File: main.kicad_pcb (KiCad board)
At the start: 2 copper layers, 100.2 x 114.2 mm, 82 parts, among them J1 Screw_Terminal_01x02, J2 Screw_Terminal_01x10, Q1 IRF540N, Q2 IRF540N, Q3 IRF540N, Q4 IRF540N, Q5 IRF540N, SW1 Arduino Reset, SW10 func3, SW11 func4, SW12 func5, SW13 Button_STOP, SW2 Switch_All, SW3 Switch1, SW4 Switch2, SW5 Switch3, SW6 Switch4, SW7 Switch5, SW8 func1, SW9 func2, U1 L7805, U2 ATmega328P-PU, U3 PC817, U4 PC817, U5 PC817, U6 PC817, U7 PC817, Y1 16mHz

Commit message: change layout
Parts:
- added H1: MountingHole, MountingHole:MountingHole_2.5mm_Pad, F.Cu at (51.6, 27.2)
- added H2: MountingHole, MountingHole:MountingHole_2.5mm_Pad, F.Cu at (135.6, 27.2)
- added H3: MountingHole, MountingHole:MountingHole_2.5mm_Pad, F.Cu at (51.6, 132.0)
- added H4: MountingHole, MountingHole:MountingHole_2.5mm_Pad, F.Cu at (135.6, 131.7)
- moved C1 57.9 mm to (65.2, 66.7)
- moved C6 57.9 mm to (65.2, 71.7)
- moved U1 57.9 mm to (70.7, 66.7)
- moved SW2 52.7 mm to (71.6, 126.7)
- moved R41 47.4 mm to (93.1, 53.1)
- moved R38 46.9 mm to (89.1, 75.7)
- moved Q5 46.9 mm to (91.0, 46.4)
- moved U7 46.9 mm to (89.2, 72.9)
- moved R39 46.9 mm to (89.1, 61.1)
- moved R40 46.9 mm to (89.1, 55.3)
- moved R42 46.9 mm to (89.1, 52.4)
- moved D5 46.9 mm to (89.1, 58.2)
- moved R18 44.9 mm to (132.7, 75.7)
- moved U3 44.9 mm to (132.7, 72.2)
- moved Q1 44.9 mm to (134.6, 46.4)
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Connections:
- J2 pad 1: /LED5 -> /LED1
- J2 pad 3: /LED4 -> /LED2
- J2 pad 7: /LED2 -> /LED4
- J2 pad 9: /LED1 -> /LED5
- SW13 pad 1: /Button_STOP -> GNDS
- SW13 pad 2: GNDS -> /Button_STOP
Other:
- board size 100.2 x 114.2 mm -> 95 x 114.2 mm
- board text added: "12V"
- board text added: "2021/09/26"
- board text added: "Arduino Reset"
- board text added: "Func Stop"
- board text added: "Func1"
- board text added: "Func2"
- board text added: "Func3"
- board text added: "Func4"
- board text added: "Func5"
- board text added: "GND"
- board text added: "LED-SW-ALL"
- board text added: "LED1"
- board text added: "LED1-SW"
- board text added: "LED1-VR"
- board text added: "LED2"
- board text added: "LED2-SW"
- board text added: "LED2-VR"
- board text added: "LED3"
- board text added: "LED3-SW"
- board text added: "LED3-VR"
- board text added: "LED4"
- board text added: "LED4-SW"
- board text added: "LED4-VR"
- board text added: "LED5"
- board text added: "LED5-SW"
- board text added: "LED5-VR"
- board text added: "TszYou Light Control Panel"

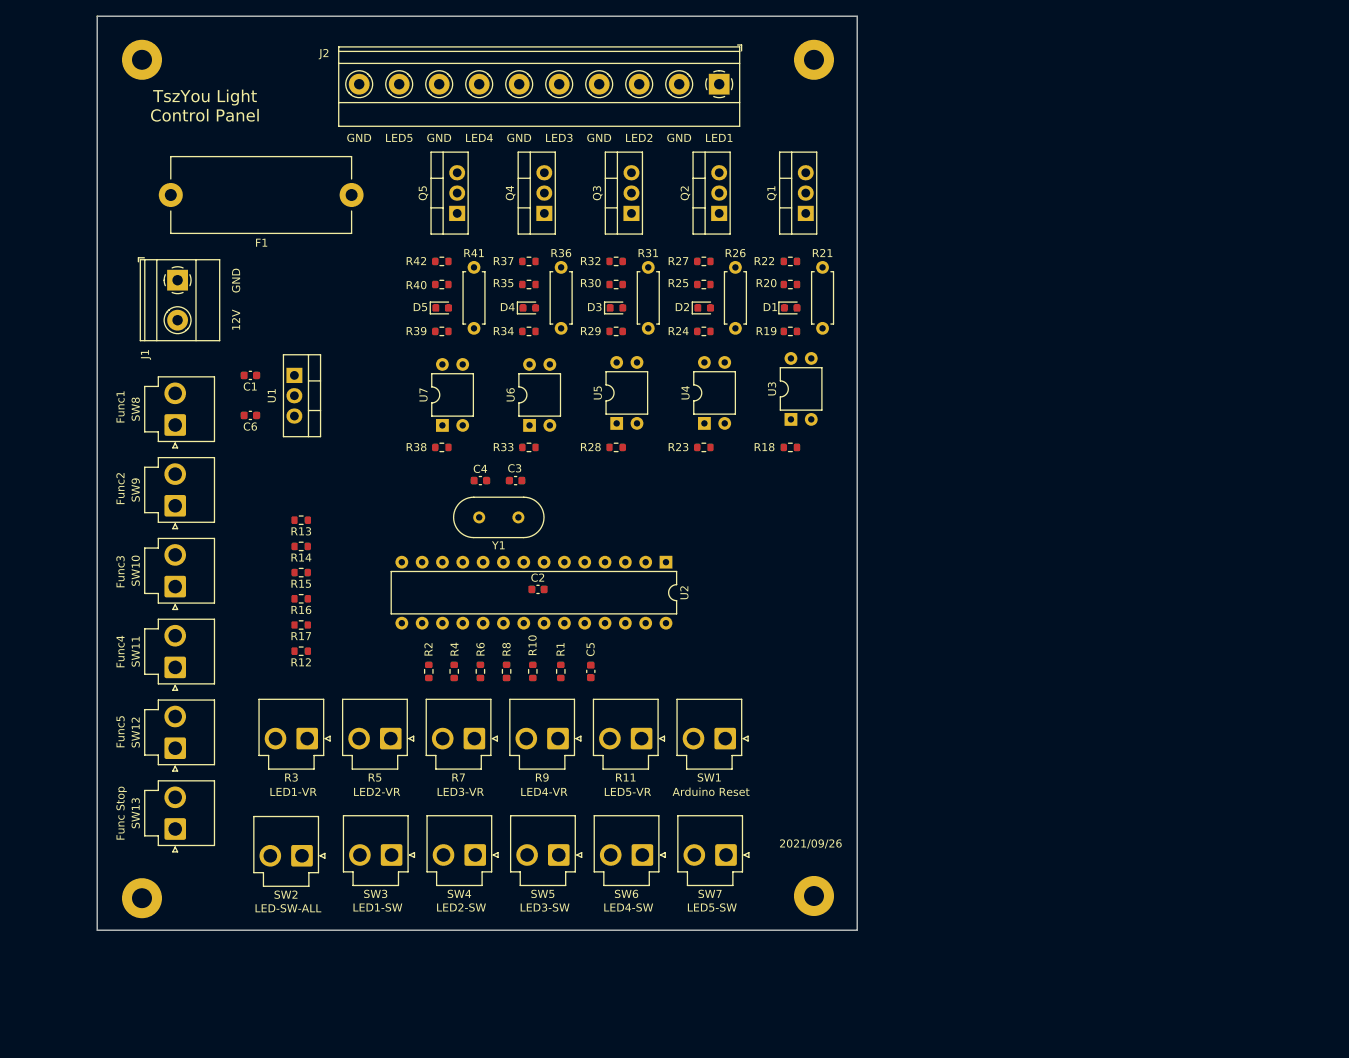
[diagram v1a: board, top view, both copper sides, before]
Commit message: [layout] complete component place
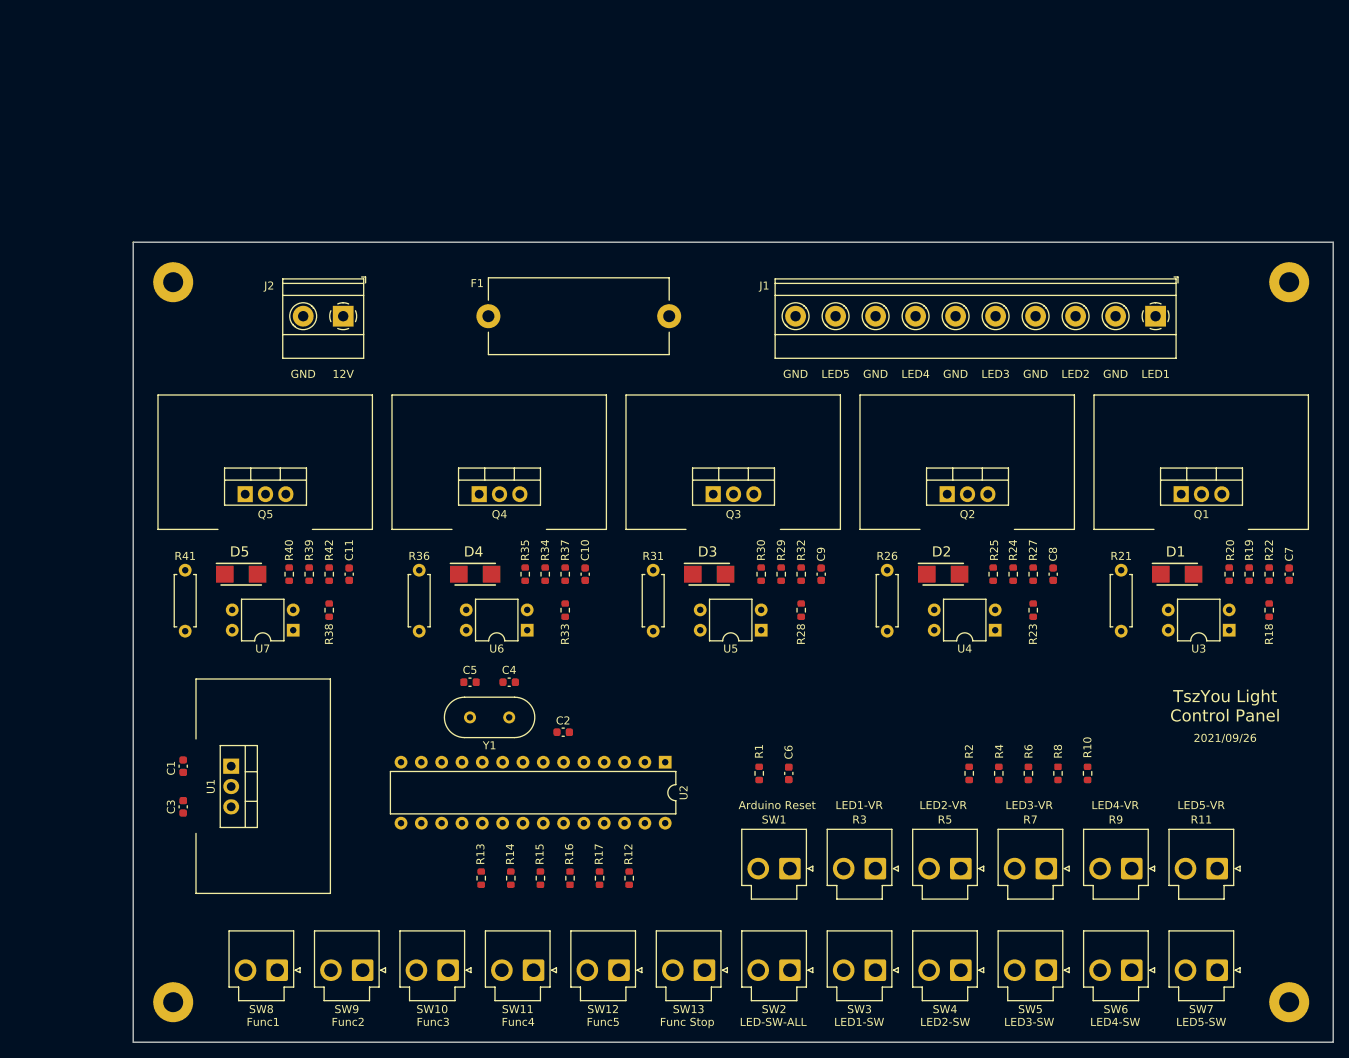
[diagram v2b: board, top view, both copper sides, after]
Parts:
- added C10: 100nF, Capacitor_SMD:C_0603_1608Metric, F.Cu at (107.0, 91.5)
- added C11: 100nF, Capacitor_SMD:C_0603_1608Metric, F.Cu at (77.5, 91.5)
- added C7: 100nF, Capacitor_SMD:C_0603_1608Metric, F.Cu at (195.0, 91.5)
- added C8: 100nF, Capacitor_SMD:C_0603_1608Metric, F.Cu at (165.5, 91.5)
- added C9: 100nF, Capacitor_SMD:C_0603_1608Metric, F.Cu at (136.5, 91.5)
- C3: value 22pF -> 0.1uF
- C5: value 0.1uF -> 22pF
- D1, D2, D3, D4, D5: footprint Diode_SMD:D_0603_1608Metric -> local_footprint:1N4007_SMD
- J1: value Screw_Terminal_01x02 -> Screw_Terminal_01x10; footprint TerminalBlock_Phoenix:TerminalBlock_Phoenix_MKDS-1,5-2_1x02_P5.00mm_Horizontal -> TerminalBlock_Phoenix:TerminalBlock_Phoenix_MKDS-1,5-10_1x10_P5.00mm_Horizontal
- J2: value Screw_Terminal_01x10 -> Screw_Terminal_01x02; footprint TerminalBlock_Phoenix:TerminalBlock_Phoenix_MKDS-1,5-10_1x10_P5.00mm_Horizontal -> TerminalBlock_Phoenix:TerminalBlock_Phoenix_MKDS-1,5-2_1x02_P5.00mm_Horizontal
- Q1, Q2, Q3, Q4, Q5: footprint Package_TO_SOT_THT:TO-220-3_Vertical -> local_footprint:TO-220_heatsink
- U1: footprint local_footprint:TO-220-3_Vertical -> local_footprint:TO-220_heatsink
- moved J1 122.3 mm to (178.3, 59.2), turned to 180 degrees
- moved C6 80.8 mm to (132.4, 116.4), turned to 90 degrees
- moved R11 73.8 mm to (186.0, 128.3)
- moved R9 73.5 mm to (175.3, 128.3)
- moved R7 73.3 mm to (164.6, 128.3)
- moved R5 73.1 mm to (154.0, 128.3)
- moved R3 72.9 mm to (143.3, 128.3)
- moved R22 71.5 mm to (192.5, 91.5), turned to 90 degrees
- moved R10 70.5 mm to (169.8, 116.4)
- moved R8 70.1 mm to (166.1, 116.4)
- moved R6 69.7 mm to (162.4, 116.4)
- moved SW8 69.3 mm to (68.5, 141.0), turned to 180 degrees
- moved R4 69.3 mm to (158.7, 116.4)
- moved R2 68.7 mm to (155.0, 116.4)
- moved SW13 68.5 mm to (121.9, 141.0), turned to 180 degrees
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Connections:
- C3 pad 1: /XTAL1 -> +5V
- C3 pad 2: GNDS -> GNDREF
- C4 pad 1: /XTAL2 -> /XTAL1
- C5 pad 1: /RESET -> /XTAL2
- C6 pad 1: +5V -> /RESET
- C6 pad 2: GNDREF -> GNDS
- J1 pad 1: GNDREF -> /LED1+
- J1 pad 2: /12V_input -> /LED1-
- J2 pad 1: /LED1 -> /12V_input
- Q1 pad 2: /LED1 -> /LED1-
- Q2 pad 2: /LED2 -> /LED2-
- Q3 pad 2: /LED3 -> /LED3-
- Q4 pad 2: /LED4 -> /LED4-
- Q5 pad 2: /LED5 -> /LED5-
- R22 pad 2: /LED1 -> /LED1+
- R27 pad 2: /LED2 -> /LED2+
- R32 pad 2: /LED3 -> /LED3+
- R37 pad 2: /LED4 -> /LED4+
- R42 pad 2: /LED5 -> /LED5+
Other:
- board size 95 x 114.2 mm -> 150 x 100 mm

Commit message: [layout] complete 90%
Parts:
- added CON1: connection, local_footprint:connect_1206_1mm, F.Cu at (58.0, 104.5)
- added J3: Conn_01x03, Connector_PinHeader_2.54mm:PinHeader_1x03_P2.54mm_Vertical, F.Cu at (83.0, 119.4)
- added R12: 3k, Resistor_SMD:R_0603_1608Metric, F.Cu at (166.1, 116.5)
- added R3: 47k, local_footprint:JST_VH_B2P-VH_1x02_P3.96mm_Vertical, F.Cu at (132.1, 128.2)
- moved U2 39.5 mm to (77.5, 115.2), turned to 90 degrees
- moved C5 21.7 mm to (101.7, 124.8), turned to 180 degrees
- moved C4 19.8 mm to (96.8, 124.8), turned to 0 degrees
- moved C2 14.5 mm to (92.0, 119.0), turned to 90 degrees
- moved BTN1 11.2 mm to (121.4, 128.3)
- moved Y1 11.0 mm to (96.8, 120.3), turned to 0 degrees
- moved R14 10.6 mm to (102.0, 131.0)
- moved R15 10.6 mm to (83.5, 131.0)
- moved R16 10.6 mm to (87.2, 131.0)
- moved R17 10.6 mm to (90.9, 131.0)
- moved R18 10.6 mm to (94.6, 131.0)
- moved R19 10.6 mm to (98.3, 131.0)
- moved R10 7.45 mm to (162.3, 116.5)
- moved R6 7.45 mm to (154.9, 116.5)
- moved R2 7.45 mm to (147.6, 116.5)
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- renumbered SW1 to BTN1, SW8 to BTN2, SW9 to BTN3, SW10 to BTN4, SW11 to BTN5, SW12 to BTN6, SW13 to BTN7, R9 to R11, R11 to R13, R12 to R14, R13 to R15, R14 to R16, R15 to R17, R16 to R18, R17 to R19, R18 to R20, R19 to R21, R20 to R22, R21 to R23, R22 to R24, R23 to R25, R24 to R26, R25 to R27, R26 to R28, R27 to R29, R28 to R30, R29 to R31, R30 to R32, R31 to R33, R32 to R34, R33 to R35, R34 to R36, R35 to R37, R36 to R38, R37 to R39, R38 to R40, R39 to R41, R40 to R42, R41 to R43, R42 to R44, R3 to R5, R5 to R7, R7 to R9
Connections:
- R10 pad 1: /ADC5 -> /ADC4
- R14 pad 1: /Button_STOP -> +5V
- R14 pad 2: +5V -> /Button_STOP
- R2 pad 1: /ADC1 -> /ADC_All
- R4 pad 1: /ADC2 -> /ADC1
- R6 pad 1: /ADC3 -> /ADC2
- R8 pad 1: /ADC4 -> /ADC3
- SW2 pad 1: +5V -> Net-(R2-Pad2)
- SW2 pad 2: Net-(SW2-Pad2) -> +5V
- SW3 pad 1: Net-(SW2-Pad2) -> Net-(R2-Pad2)
- SW3 pad 2: Net-(R2-Pad2) -> Net-(R4-Pad2)
- SW4 pad 1: Net-(SW2-Pad2) -> Net-(R2-Pad2)
- SW4 pad 2: Net-(R4-Pad2) -> Net-(R6-Pad2)
- SW5 pad 1: Net-(SW2-Pad2) -> Net-(R2-Pad2)
- SW5 pad 2: Net-(R6-Pad2) -> Net-(R8-Pad2)
- SW6 pad 1: Net-(SW2-Pad2) -> Net-(R2-Pad2)
- SW6 pad 2: Net-(R8-Pad2) -> Net-(R10-Pad2)
- SW7 pad 1: Net-(SW2-Pad2) -> Net-(R2-Pad2)
- SW7 pad 2: Net-(R10-Pad2) -> Net-(R12-Pad2)
- U2 pad 11: Net-(U2-Pad11) -> /PWM2
- U2 pad 12: Net-(U2-Pad12) -> /PWM1
- U2 pad 13: Net-(U2-Pad13) -> /func4
- U2 pad 14: /func1 -> /func5
- U2 pad 15: /func2 -> /PWM3
- U2 pad 16: /func3 -> /PWM4
- U2 pad 17: /func4 -> /PWM5
- U2 pad 18: /func5 -> Net-(U2-Pad18)
- U2 pad 2: /PWM1 -> /RXD
- U2 pad 23: /ADC1 -> /ADC5
- U2 pad 24: /ADC2 -> /ADC4
- U2 pad 26: /ADC4 -> /ADC2
- U2 pad 27: /ADC5 -> /ADC1
- U2 pad 28: /Button_All -> /ADC_All
- U2 pad 3: /PWM2 -> /TXD
- U2 pad 4: /PWM3 -> /func1
- U2 pad 5: /PWM4 -> /func2
- U2 pad 6: /PWM5 -> /func3
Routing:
- net +12V: track 0.00 -> 374.1 mm, vias 0 -> 5
- net +5V: track 0.00 -> 220.5 mm
- net Net-(R2-Pad2): track 0.00 -> 109.6 mm
- net /ADC5: track 0.00 -> 104.1 mm
- net /ADC4: track 0.00 -> 95.8 mm
- net /ADC_All: track 0.00 -> 94.3 mm
- net /PWM1: track 0.00 -> 93.9 mm, vias 0 -> 1
- net /ADC3: track 0.00 -> 91.8 mm
- net /ADC1: track 0.00 -> 90.7 mm
- net /ADC2: track 0.00 -> 88.9 mm
- net /LED5-: track 0.00 -> 82.7 mm
- net /LED5+: track 0.00 -> 77.6 mm
- net /RESET: track 0.00 -> 68.3 mm
- net /PWM2: track 0.00 -> 67.7 mm, vias 0 -> 1
- net /LED4-: track 0.00 -> 64.0 mm
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- added copper zone on B.Cu, net GNDREF
- added copper zone on F.Cu, net GNDREF
- added copper zone on B.Cu, net GNDS
- added copper zone on F.Cu, net GNDS
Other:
- outline, holes or cut-outs redrawn
- board text added: "LED_All-SW"
- board text added: "LED_All-VR"
- board text added: "RXD"
- board text added: "TXD"
- board text removed: "LED-SW-ALL"

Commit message: [layout] completed
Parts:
- removed CON1: connection, local_footprint:connect_1206_1mm
- added JP1: Jumper_2_Bridged, local_footprint:connect_1206_1mm, F.Cu at (58.0, 104.8)
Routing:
- net +12V: track 374.1 -> 375.9 mm
